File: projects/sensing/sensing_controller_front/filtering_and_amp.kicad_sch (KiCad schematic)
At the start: 21 parts, among them U4 AD8630

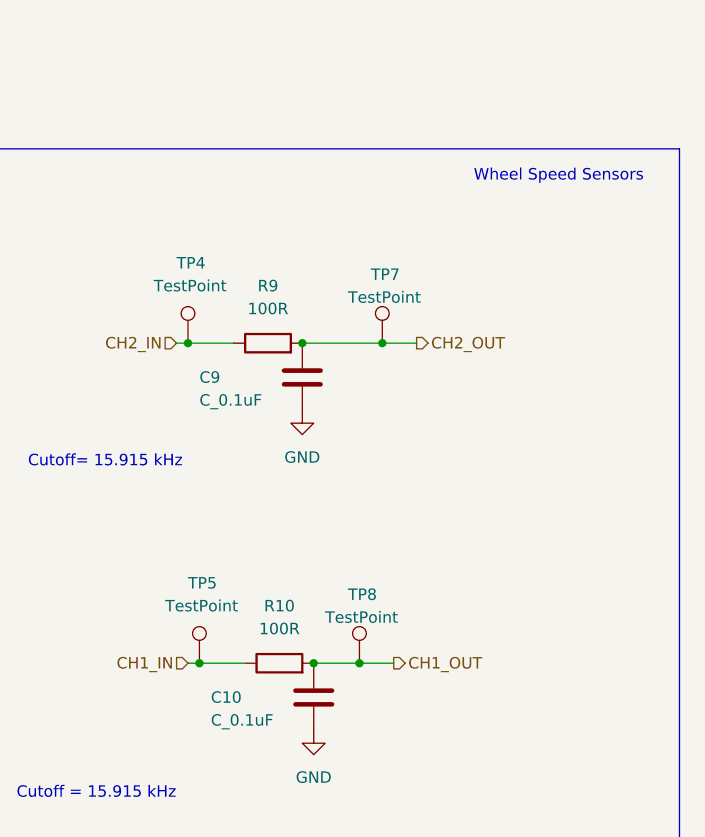
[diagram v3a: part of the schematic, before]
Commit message: added pull-up resistor
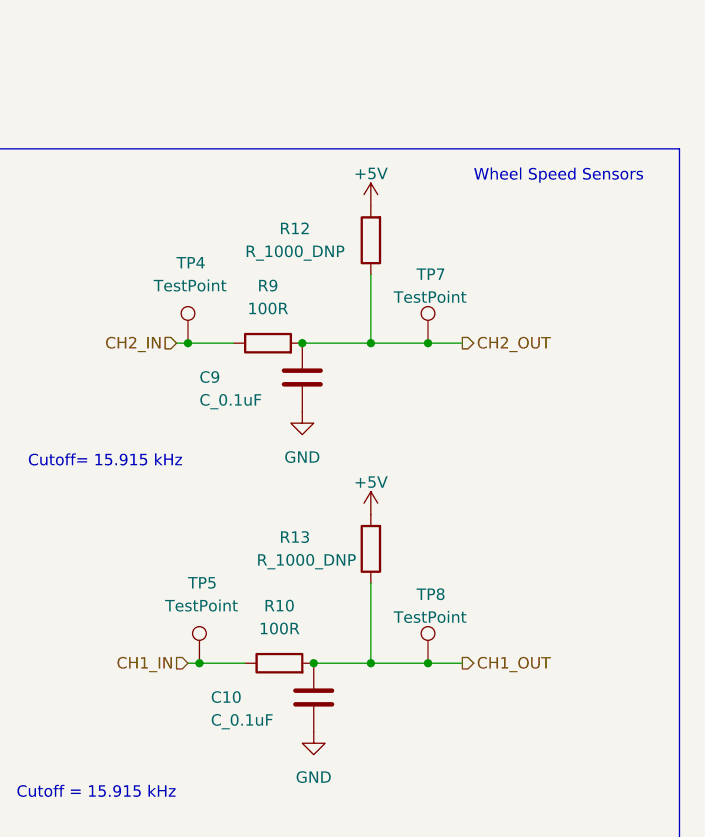
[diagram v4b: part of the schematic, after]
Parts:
- added R12, R13: R_1000_DNP, OEM:R_0603, symbol formula:R_200
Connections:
- net +5V: now also R12.2, R13.2
- net CH1_OUT: now also R13.1
- net CH2_OUT: now also R12.1
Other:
- moved on the sheet: TP7, TP8
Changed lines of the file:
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@@
   (junction (at 121.92 82.55) (diameter 0) (color 0 0 0 0)
   )
-  (junction (at 242.57 91.44) (diameter 0) (color 0 0 0 0)
+  (junction (at 241.3 91.44) (diameter 0) (color 0 0 0 0)
+  )
+  (junction (at 247.65 91.44) (diameter 0) (color 0 0 0 0)
   )
   (junction (at 233.68 91.44) (diameter 0) (color 0 0 0 0)
   )
+  (junction (at 241.3 127) (diameter 0) (color 0 0 0 0)
+  )
   (junction (at 220.98 91.44) (diameter 0) (color 0 0 0 0)
   )
@@
   (junction (at 234.95 127) (diameter 0) (color 0 0 0 0)
   )
-  (junction (at 240.03 127) (diameter 0) (color 0 0 0 0)
+  (junction (at 247.65 127) (diameter 0) (color 0 0 0 0)
   )
   (junction (at 133.35 125.73) (diameter 0) (color 0 0 0 0)
@@
     (stroke (width 0) (type default) (color 0 0 0 0))
   )
-  (wire (pts (xy 246.38 91.44) (xy 242.57 91.44))
+  (wire (pts (xy 251.46 91.44) (xy 247.65 91.44))
     (stroke (width 0) (type default) (color 0 0 0 0))
   )
@@
     (stroke (width 0) (type default) (color 0 0 0 0))
   )
-  (wire (pts (xy 233.68 91.44) (xy 242.57 91.44))
-    (stroke (width 0) (type default) (color 0 0 0 0))
-  )
   (polyline (pts (xy 184.15 67.31) (xy 184.15 74.93))
     (stroke (width 0) (type default) (color 0 0 0 0))
@@
     (stroke (width 0) (type default) (color 0 0 0 0))
   )
+  (wire (pts (xy 241.3 127) (xy 247.65 127))
+    (stroke (width 0) (type default) (color 0 0 0 0))
+  )
   (polyline (pts (xy 198.12 21.59) (xy 180.34 21.59))
     (stroke (width 0) (type default) (color 0 0 0 0))
@@
     (stroke (width 0) (type default) (color 0 0 0 0))
   )
+  (wire (pts (xy 241.3 91.44) (xy 247.65 91.44))
+    (stroke (width 0) (type default) (color 0 0 0 0))
+  )
   (wire (pts (xy 120.65 82.55) (xy 121.92 82.55))
     (stroke (width 0) (type default) (color 0 0 0 0))
@@
     (stroke (width 0) (type default) (color 0 0 0 0))
   )
-  (wire (pts (xy 234.95 127) (xy 240.03 127))
-    (stroke (width 0) (type default) (color 0 0 0 0))
-  )
   (polyline (pts (xy 193.04 154.94) (xy 275.59 154.94))
     (stroke (width 0) (type default) (color 0 0 0 0))
@@
     (stroke (width 0) (type default) (color 0 0 0 0))
   )
+  (wire (pts (xy 234.95 127) (xy 241.3 127))
+    (stroke (width 0) (type default) (color 0 0 0 0))
+  )
   (wire (pts (xy 120.65 125.73) (xy 125.73 125.73))
     (stroke (width 0) (type default) (color 0 0 0 0))
@@
     (stroke (width 0) (type default) (color 0 0 0 0))
   )
+  (wire (pts (xy 241.3 83.82) (xy 241.3 91.44))
+    (stroke (width 0) (type default) (color 0 0 0 0))
+  )
   (wire (pts (xy 220.98 127) (xy 222.25 127))
     (stroke (width 0) (type default) (color 0 0 0 0))
   )
-  (wire (pts (xy 243.84 127) (xy 240.03 127))
+  (wire (pts (xy 241.3 118.11) (xy 241.3 127))
+    (stroke (width 0) (type default) (color 0 0 0 0))
+  )
+  (wire (pts (xy 251.46 127) (xy 247.65 127))
     (stroke (width 0) (type default) (color 0 0 0 0))
   )
@@
   )
   (wire (pts (xy 139.7 97.79) (xy 146.05 97.79))
+    (stroke (width 0) (type default) (color 0 0 0 0))
+  )
+  (wire (pts (xy 233.68 91.44) (xy 241.3 91.44))
     (stroke (width 0) (type default) (color 0 0 0 0))
   )
@@
     (effects (font (size 1.27 1.27)) (justify left))
   )
-  (hierarchical_label "CH2_OUT" (shape output) (at 246.38 91.44 0)
+  (hierarchical_label "CH2_OUT" (shape output) (at 251.46 91.44 0)
     (effects (font (size 1.27 1.27)) (justify left))
   )
@@
     (effects (font (size 1.27 1.27)) (justify right))
   )
-  (hierarchical_label "CH1_OUT" (shape output) (at 243.84 127 0)
+  (hierarchical_label "CH1_OUT" (shape output) (at 251.46 127 0)
     (effects (font (size 1.27 1.27)) (justify left))
   )
@@
     (pin "1")
   )
+  (symbol (lib_id "power:+5V") (at 241.3 110.49 0) (unit 1)
+    (in_bom yes) (on_board yes) (fields_autoplaced)
+    (property "Reference" "#PWR?" (id 0) (at 241.3 114.3 0)
+      (effects (font (size 1.27 1.27)) hide)
+    )
+    (property "Value" "+5V" (id 1) (at 241.3 106.9142 0))
+    (property "Footprint" "" (id 2) (at 241.3 110.49 0)
+      (effects (font (size 1.27 1.27)) hide)
+    )
+    (property "Datasheet" "" (id 3) (at 241.3 110.49 0)
+      (effects (font (size 1.27 1.27)) hide)
+    )
+    (pin "1")
+  )
+  (symbol (lib_id "formula:R_200") (at 241.3 80.01 180) (unit 1)
+    (in_bom yes) (on_board yes)
+    (property "Reference" "R12" (id 0) (at 231.14 78.74 0)
+      (effects (font (size 1.27 1.27)) (justify right))
+    )
+    (property "Value" "R_1000_DNP" (id 1) (at 227.33 81.28 0)
+      (effects (font (size 1.27 1.27)) (justify right))
+    )
+    (property "Footprint" "OEM:R_0603" (id 2) (at 243.078 80.01 0)
+      (effects (font (size 1.27 1.27)) hide)
+    )
+    (property "Datasheet" "https://www.seielect.com/Catalog/SEI-RMCF_RMCP.pdf" (id 3) (at 239.268 80.01 0)
+      (effects (font (size 1.27 1.27)) hide)
+    )
+    (property "MFN" "DK" (id 4) (at 241.3 80.01 0)
+      (effects (font (size 1.524 1.524)) hide)
+    )
+    (property "MPN" "RMCF0805JT200RCT-ND" (id 5) (at 241.3 80.01 0)
+      (effects (font (size 1.524 1.524)) hide)
+    )
+    (property "PurchasingLink" "https://www.digikey.com/products/en?keywords=RMCF0805JT200RCT-ND" (id 6) (at 229.108 90.17 0)
+      (effects (font (size 1.524 1.524)) hide)
+    )
+    (pin "1")
+    (pin "2")
+  )
   (symbol (lib_id "Connector:TestPoint") (at 167.64 85.09 0) (unit 1)
     (in_bom yes) (on_board yes)
@@
     (pin "1")
   )
-  (symbol (lib_id "Connector:TestPoint") (at 242.57 91.44 0) (unit 1)
-    (in_bom yes) (on_board yes)
-    (property "Reference" "TP7" (id 0) (at 241.3 83.82 0)
-      (effects (font (size 1.27 1.27)) (justify left))
-    )
-    (property "Value" "TestPoint" (id 1) (at 238.76 86.36 0)
-      (effects (font (size 1.27 1.27)) (justify left))
-    )
-    (property "Footprint" "" (id 2) (at 247.65 91.44 0)
-      (effects (font (size 1.27 1.27)) hide)
-    )
-    (property "Datasheet" "~" (id 3) (at 247.65 91.44 0)
+  (symbol (lib_id "Connector:TestPoint") (at 247.65 91.44 0) (unit 1)
+    (in_bom yes) (on_board yes)
+    (property "Reference" "TP7" (id 0) (at 246.38 83.82 0)
+      (effects (font (size 1.27 1.27)) (justify left))
+    )
+    (property "Value" "TestPoint" (id 1) (at 243.84 86.36 0)
+      (effects (font (size 1.27 1.27)) (justify left))
+    )
+    (property "Footprint" "" (id 2) (at 252.73 91.44 0)
+      (effects (font (size 1.27 1.27)) hide)
+    )
+    (property "Datasheet" "~" (id 3) (at 252.73 91.44 0)
       (effects (font (size 1.27 1.27)) hide)
     )
@@
     (pin "2")
   )
+  (symbol (lib_id "power:+5V") (at 241.3 76.2 0) (unit 1)
+    (in_bom yes) (on_board yes) (fields_autoplaced)
+    (property "Reference" "#PWR?" (id 0) (at 241.3 80.01 0)
+      (effects (font (size 1.27 1.27)) hide)
+    )
+    (property "Value" "+5V" (id 1) (at 241.3 72.6242 0))
+    (property "Footprint" "" (id 2) (at 241.3 76.2 0)
+      (effects (font (size 1.27 1.27)) hide)
+    )
+    (property "Datasheet" "" (id 3) (at 241.3 76.2 0)
+      (effects (font (size 1.27 1.27)) hide)
+    )
+    (pin "1")
+  )
   (symbol (lib_id "Connector:TestPoint") (at 166.37 128.27 0) (unit 1)
     (in_bom yes) (on_board yes)
@@
   )
   (symbol (lib_id "OEM:100R") (at 231.14 127 90) (unit 1)
-    (in_bom yes) (on_board yes) (fields_autoplaced)
+    (in_bom yes) (on_board yes)
     (property "Reference" "R10" (id 0) (at 231.14 120.65 90))
     (property "Value" "100R" (id 1) (at 231.14 123.19 90))
@@
     (pin "2")
   )
-  (symbol (lib_id "Connector:TestPoint") (at 240.03 127 0) (unit 1)
-    (in_bom yes) (on_board yes)
-    (property "Reference" "TP8" (id 0) (at 238.76 119.38 0)
-      (effects (font (size 1.27 1.27)) (justify left))
-    )
-    (property "Value" "TestPoint" (id 1) (at 236.22 121.92 0)
-      (effects (font (size 1.27 1.27)) (justify left))
-    )
-    (property "Footprint" "" (id 2) (at 245.11 127 0)
-      (effects (font (size 1.27 1.27)) hide)
-    )
-    (property "Datasheet" "~" (id 3) (at 245.11 127 0)
-      (effects (font (size 1.27 1.27)) hide)
-    )
+  (symbol (lib_id "formula:R_200") (at 241.3 114.3 180) (unit 1)
+    (in_bom yes) (on_board yes)
+    (property "Reference" "R13" (id 0) (at 231.14 113.03 0)
+      (effects (font (size 1.27 1.27)) (justify right))
+    )
+    (property "Value" "R_1000_DNP" (id 1) (at 228.6 115.57 0)
+      (effects (font (size 1.27 1.27)) (justify right))
+    )
+    (property "Footprint" "OEM:R_0603" (id 2) (at 243.078 114.3 0)
+      (effects (font (size 1.27 1.27)) hide)
+    )
+    (property "Datasheet" "https://www.seielect.com/Catalog/SEI-RMCF_RMCP.pdf" (id 3) (at 239.268 114.3 0)
+      (effects (font (size 1.27 1.27)) hide)
+    )
+    (property "MFN" "DK" (id 4) (at 241.3 114.3 0)
+      (effects (font (size 1.524 1.524)) hide)
+    )
+    (property "MPN" "RMCF0805JT200RCT-ND" (id 5) (at 241.3 114.3 0)
+      (effects (font (size 1.524 1.524)) hide)
+    )
+    (property "PurchasingLink" "https://www.digikey.com/products/en?keywords=RMCF0805JT200RCT-ND" (id 6) (at 229.108 124.46 0)
+      (effects (font (size 1.524 1.524)) hide)
+    )
+    (pin "1")
+    (pin "2")
+  )
+  (symbol (lib_id "Connector:TestPoint") (at 247.65 127 0) (unit 1)
+    (in_bom yes) (on_board yes)
+    (property "Reference" "TP8" (id 0) (at 246.38 119.38 0)
+      (effects (font (size 1.27 1.27)) (justify left))
+    )
+    (property "Value" "TestPoint" (id 1) (at 243.84 121.92 0)
+      (effects (font (size 1.27 1.27)) (justify left))
+    )
+    (property "Footprint" "" (id 2) (at 252.73 127 0)
+      (effects (font (size 1.27 1.27)) hide)
+    )
+    (property "Datasheet" "~" (id 3) (at 252.73 127 0)
+      (effects (font (size 1.27 1.27)) hide)
+    )

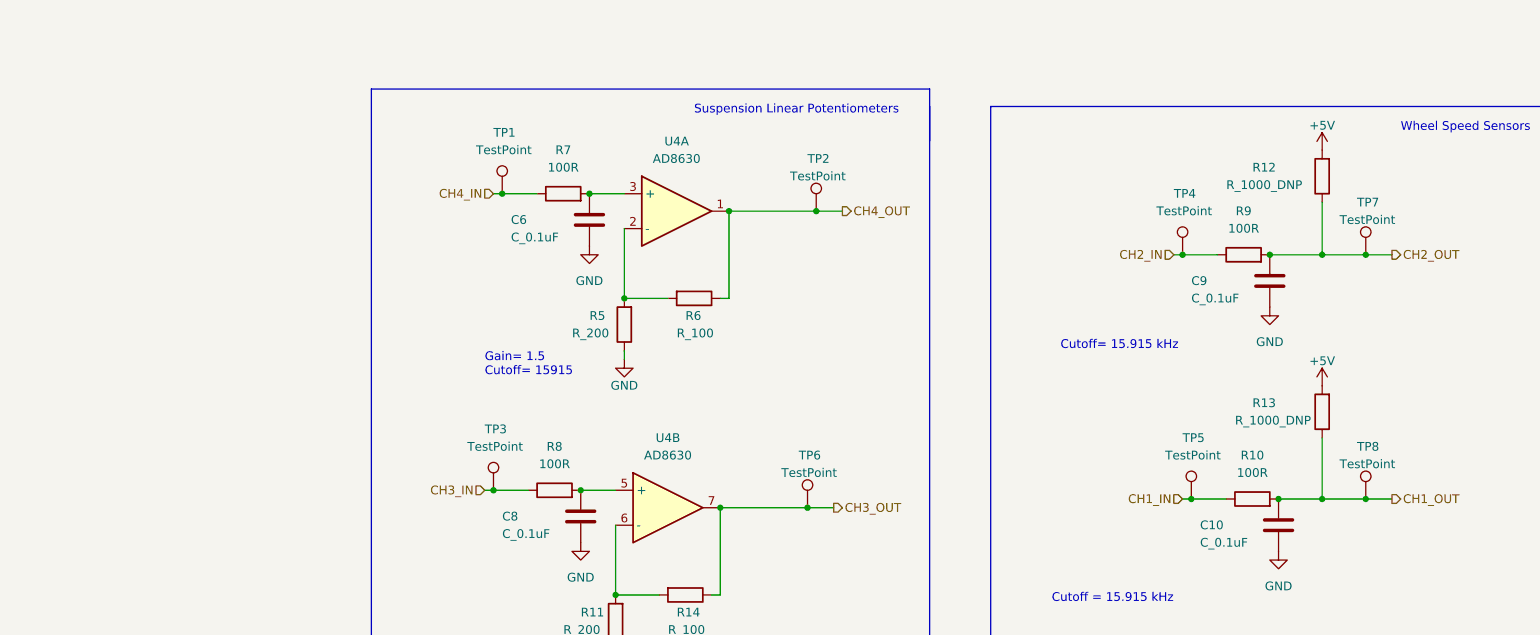
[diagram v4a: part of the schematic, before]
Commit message: added test points and completed board dimensions
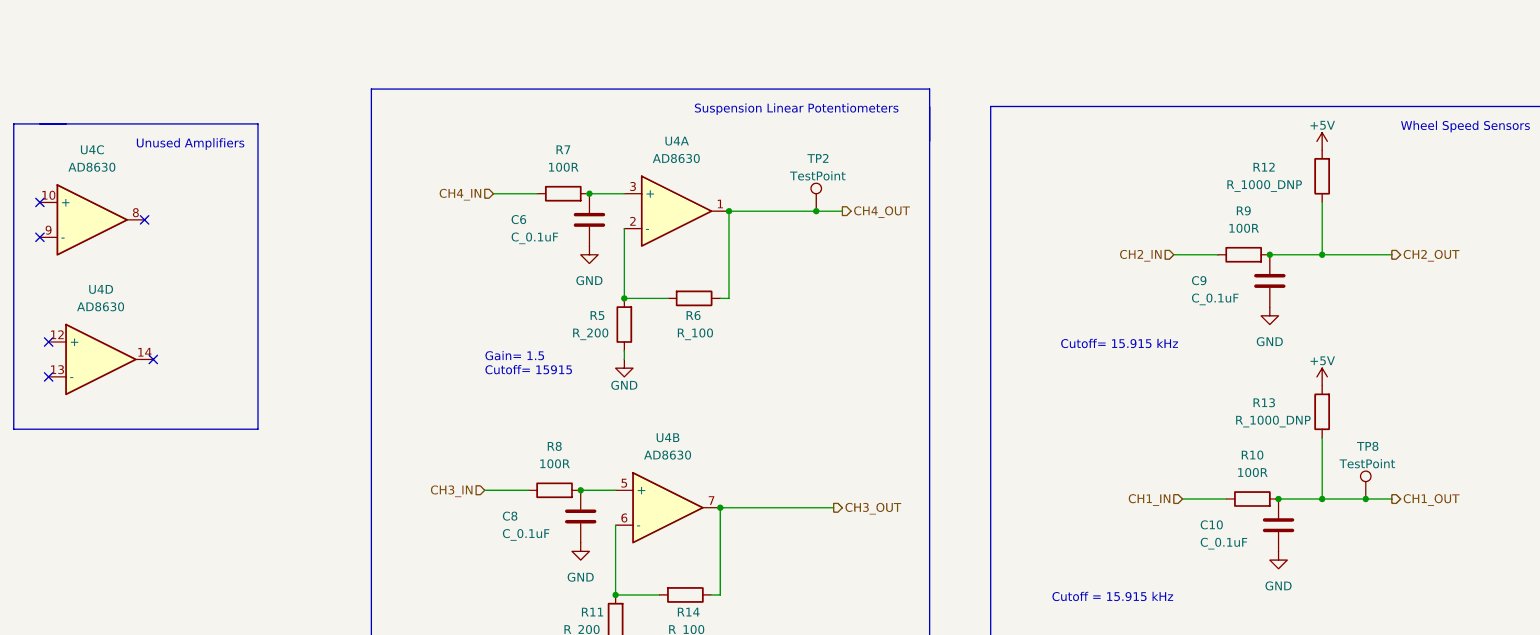
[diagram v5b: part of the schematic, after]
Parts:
- removed TP1, TP3, TP4, TP5, TP6, TP7: TestPoint, symbol Connector:TestPoint
- added unit 4 of U4
- added unit 3 of U4
- TP2: footprint TestPoint:TestPoint_Pad_D2.0mm -> TestPoint:TestPoint_Pad_D1.0mm
- TP8: footprint (none) -> TestPoint:TestPoint_Pad_D1.0mm
- U4: footprint Package_SO:SOIC-14_3.9x8.7mm_P1.27mm -> (none)
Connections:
- no-connect marks 0 -> 6
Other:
- note added: "Unused Amplifiers"
